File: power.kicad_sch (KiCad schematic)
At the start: 5 parts, among them J1 USB_C_Receptacle

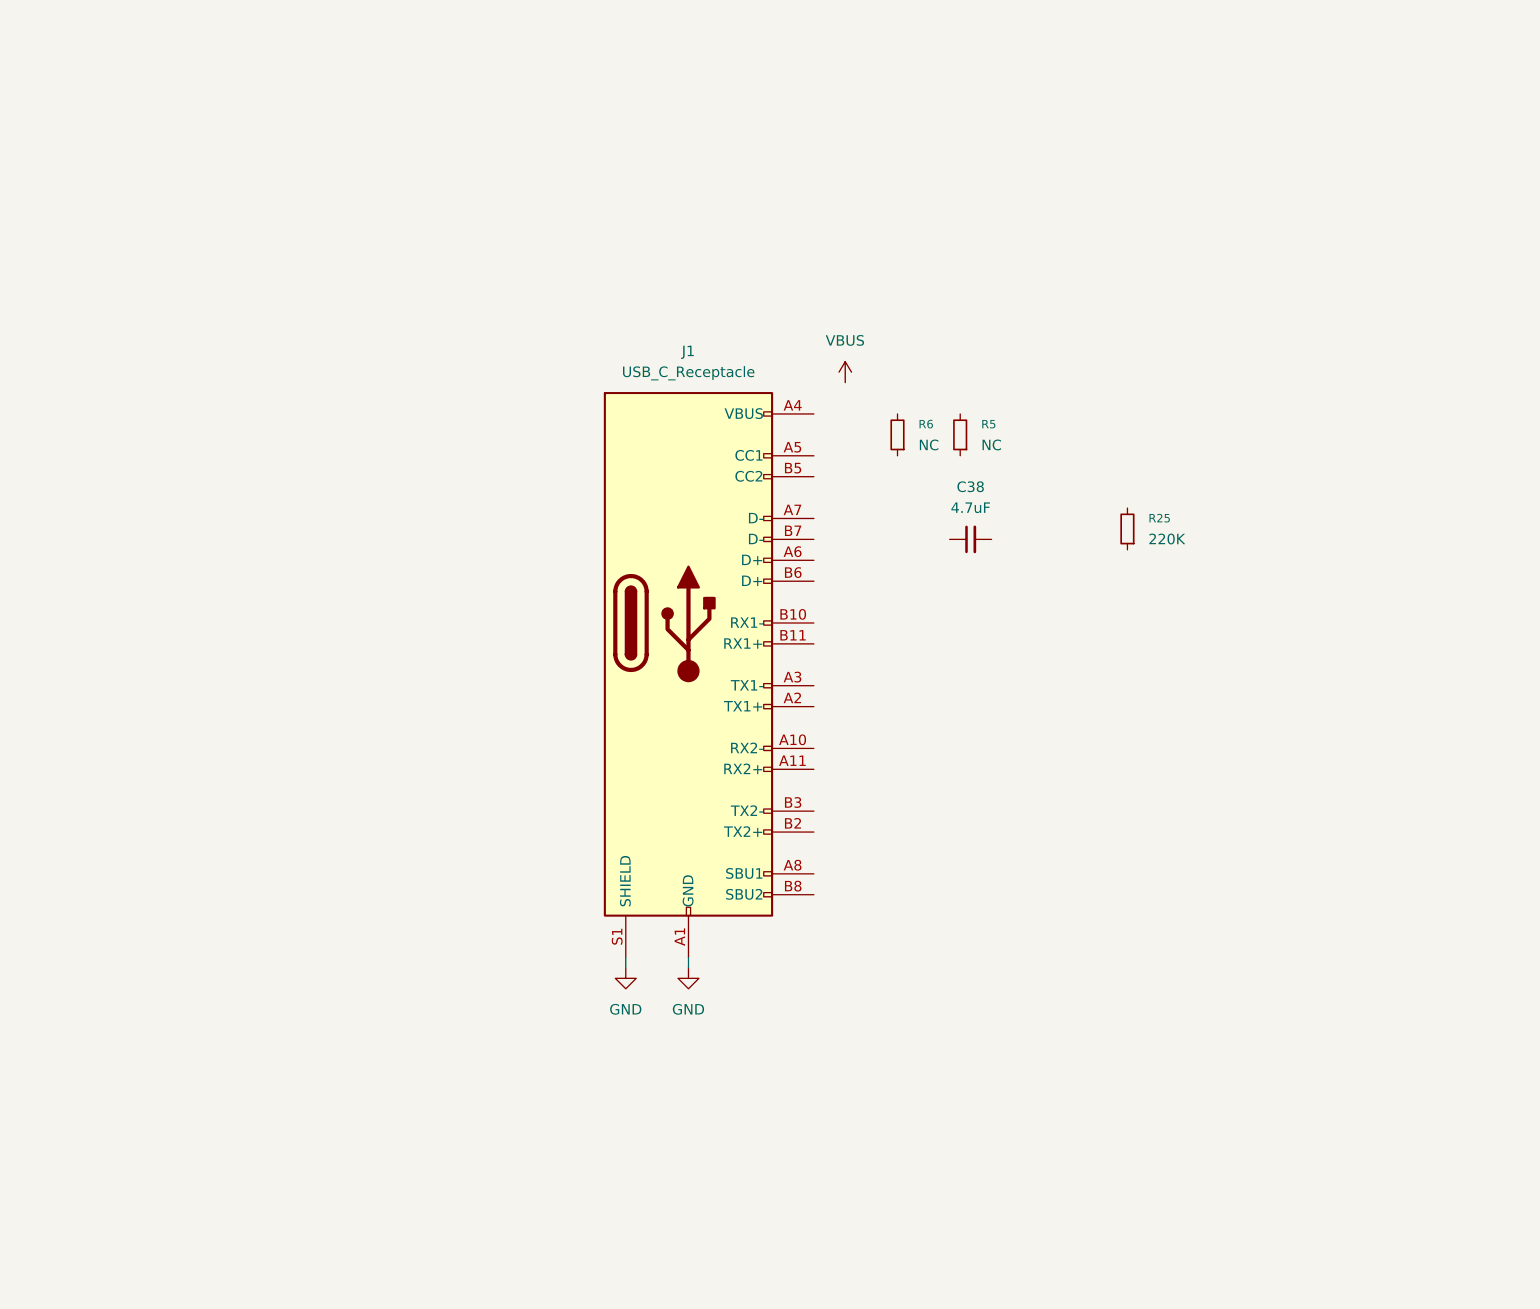
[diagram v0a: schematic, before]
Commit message: added power schematic, gitignore
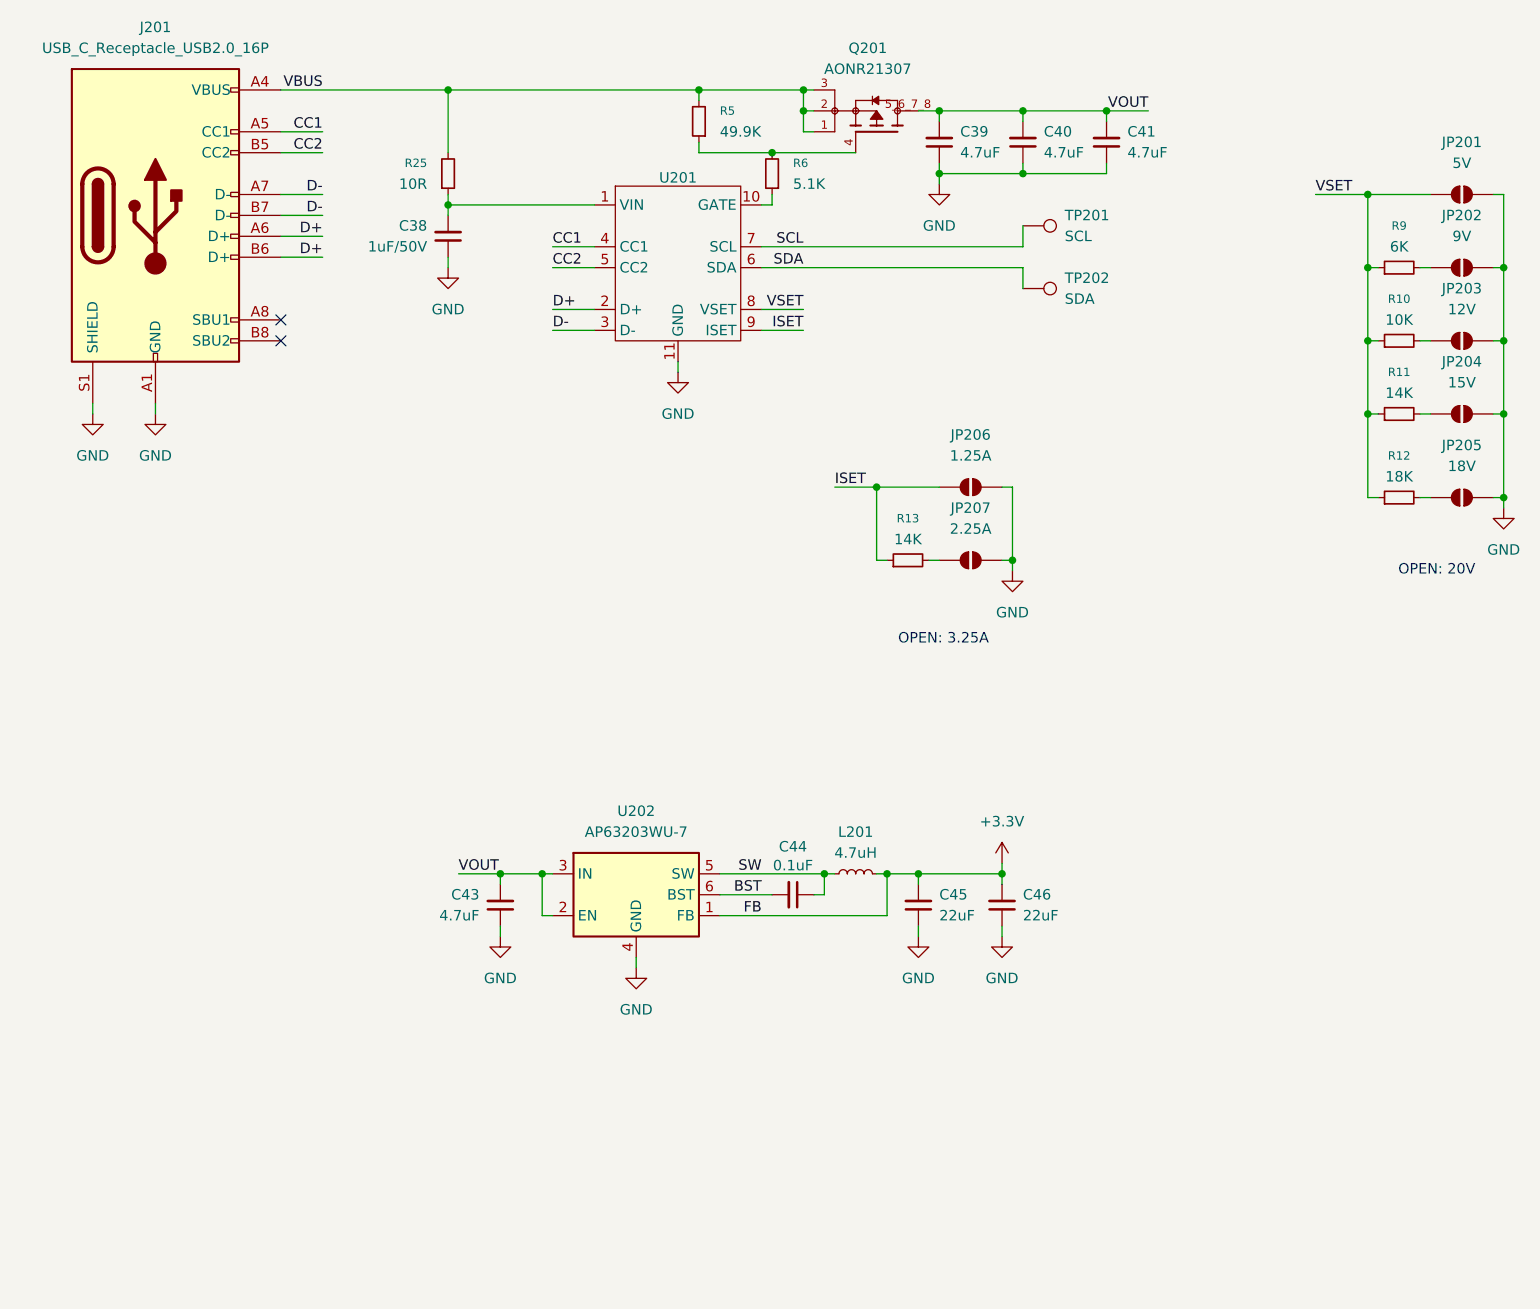
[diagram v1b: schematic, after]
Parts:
- removed J1: USB_C_Receptacle, symbol Connector:USB_C_Receptacle
- added C39, C40, C41, C43: 4.7uF, Capacitor_SMD:C_0603_1608Metric_Pad1.08x0.95mm_HandSolder, symbol Device:C_Small
- added C44: 0.1uF, Capacitor_SMD:C_0603_1608Metric_Pad1.08x0.95mm_HandSolder, symbol Device:C_Small
- added C45, C46: 22uF, Capacitor_SMD:C_0603_1608Metric_Pad1.08x0.95mm_HandSolder, symbol Device:C_Small
- added J201: USB_C_Receptacle_USB2.0_16P, SHOUHAN_TYPE-C_16PIN_2MD__073:SHOUHAN_TYPE-C_16PIN_2MD__073, symbol Connector:USB_C_Receptacle_USB2.0_16P
- added JP201: 5V, Jumper:SolderJumper-2_P1.3mm_Open_RoundedPad1.0x1.5mm, symbol Jumper:SolderJumper_2_Open
- added JP202: 9V, Jumper:SolderJumper-2_P1.3mm_Open_RoundedPad1.0x1.5mm, symbol Jumper:SolderJumper_2_Open
- added JP203: 12V, Jumper:SolderJumper-2_P1.3mm_Open_RoundedPad1.0x1.5mm, symbol Jumper:SolderJumper_2_Open
- added JP204: 15V, Jumper:SolderJumper-2_P1.3mm_Open_RoundedPad1.0x1.5mm, symbol Jumper:SolderJumper_2_Open
- added JP205: 18V, Jumper:SolderJumper-2_P1.3mm_Open_RoundedPad1.0x1.5mm, symbol Jumper:SolderJumper_2_Open
- added JP206: 1.25A, Jumper:SolderJumper-2_P1.3mm_Open_RoundedPad1.0x1.5mm, symbol Jumper:SolderJumper_2_Open
- added JP207: 2.25A, Jumper:SolderJumper-2_P1.3mm_Open_RoundedPad1.0x1.5mm, symbol Jumper:SolderJumper_2_Open
- added L201: 4.7uH, symbol Device:L_Small
- added Q201: AONR21307, AONR21307:AONR21307, symbol AONR21307:AONR21307
- added R10: 10K, Resistor_SMD:R_0603_1608Metric_Pad0.98x0.95mm_HandSolder, symbol Device:R_Small
- added R11, R13: 14K, Resistor_SMD:R_0603_1608Metric_Pad0.98x0.95mm_HandSolder, symbol Device:R_Small
- added R12: 18K, Resistor_SMD:R_0603_1608Metric_Pad0.98x0.95mm_HandSolder, symbol Device:R_Small
- added R9: 6K, Resistor_SMD:R_0603_1608Metric_Pad0.98x0.95mm_HandSolder, symbol Device:R_Small
- added TP201: SCL, TestPoint:TestPoint_Pad_D1.5mm, symbol Connector:TestPoint
- added TP202: SDA, TestPoint:TestPoint_Pad_D1.5mm, symbol Connector:TestPoint
- added U201: ~, Package_DFN_QFN:DFN-10-1EP_3x3mm_P0.5mm_EP1.55x2.48mm, symbol HUSB238_002DD:HUSB238_002DD
- added U202: AP63203WU-7, Package_TO_SOT_SMD:TSOT-23-6, symbol Regulator_Switching:AP63203WU
- C38: value 4.7uF -> 1uF/50V
- R25: value 220K -> 10R
- R5: value NC -> 49.9K
- R6: value NC -> 5.1K
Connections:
- net GND: now also C38.1, C39.1, C40.1, C41.1, C43.1, C45.1, C46.1, J201.A1 (GND), J201.A12 (GND), J201.B1 (GND), J201.B12 (GND), J201.S1 (SHIELD), JP201.2 (B), JP202.2 (B), JP203.2 (B), JP204.2 (B), JP205.2 (B), JP206.2 (B), JP207.2 (B), U201.11 (GND), U202.4 (GND)
- net VBUS: now also R25.2, R5.2, J201.A4 (VBUS), J201.A9 (VBUS), J201.B4 (VBUS), J201.B9 (VBUS), Q201.1, Q201.2, Q201.3
- net at R5.1: now also R6.2, Q201.4
- net at R25.1: now also C38.2, U201.1 (VIN)
- net at R6.1: now also U201.10 (GATE)
- new net: JP204.1 (A), R11.2
- new net: JP207.1 (A), R13.2
- new net: JP203.1 (A), R10.2
- new net: JP202.1 (A), R9.2
- new net: JP205.1 (A), R12.2
- new net +3.3V: C45.2, C46.2, L201.2, U202.1 (FB)
- new net BST: C44.2, U202.6 (BST)
- new net CC1: J201.A5 (CC1), U201.4 (CC1)
- new net CC2: J201.B5 (CC2), U201.5 (CC2)
- new net D+: J201.A6 (D+), J201.B6 (D+), U201.2 (D+)
- new net D-: J201.A7 (D-), J201.B7 (D-), U201.3 (D-)
- new net ISET: JP206.1 (A), R13.1, U201.9 (ISET)
- new net SCL: TP201.1, U201.7 (SCL)
- new net SDA: TP202.1, U201.6 (SDA)
- new net SW: C44.1, L201.1, U202.5 (SW)
- new net VOUT: C39.2, C40.2, C41.2, C43.2, Q201.5_6_7_8, U202.2 (EN), U202.3 (IN)
- new net VSET: JP201.1 (A), R10.1, R11.1, R12.1, R9.1, U201.8 (VSET)
- no-connect marks 0 -> 2
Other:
- note added: "OPEN: 20V"
- note added: "OPEN: 3.25A"
- moved on the sheet: C38, R25, R5, R6

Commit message: power section done
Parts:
- L201: value 4.7uH -> 10uH; footprint (none) -> VLS5045EX-100M:VLS5045EX330M
- U201: value ~ -> HUSB238_002DD; footprint Package_DFN_QFN:DFN-10-1EP_3x3mm_P0.5mm_EP1.55x2.48mm -> Package_DFN_QFN:DFN-10-1EP_3x3mm_P0.5mm_EP1.65x2.38mm_ThermalVias
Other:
- note added: "TDK, VLS5045EX-100M"
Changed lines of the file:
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@@
+		)
+	)
+	(text "TDK, VLS5045EX-100M"
+		(exclude_from_sim no)
+		(at 115.57 113.284 0)
+		(effects
+			(font
+				(size 1.27 1.27)
+			)
 		)
 	)
@@
 	)
 	(symbol
+		(lib_id "HUSB238_002DD:HUSB238_002DD")
+		(at 93.98 45.72 0)
+		(unit 1)
+		(exclude_from_sim no)
+		(in_bom yes)
+		(on_board yes)
+		(dnp no)
+		(property "Reference" "U201"
+			(at 93.98 33.782 0)
+			(effects
+				(font
+					(size 1.27 1.27)
+				)
+			)
+		)
+		(property "Value" "HUSB238_002DD"
+			(at 93.98 35.814 0)
+			(effects
+				(font
+					(size 1.27 1.27)
+				)
+			)
+		)
+		(property "Footprint" "Package_DFN_QFN:DFN-10-1EP_3x3mm_P0.5mm_EP1.65x2.38mm_ThermalVias"
+			(at 93.98 45.72 0)
+			(effects
+				(font
+					(size 1.27 1.27)
+				)
+				(hide yes)
+			)
+		)
+		(property "Datasheet" ""
+			(at 93.98 45.72 0)
+			(effects
+				(font
+					(size 1.27 1.27)
+				)
+				(hide yes)
+			)
+		)
+		(property "Description" ""
+			(at 93.98 45.72 0)
+			(effects
+				(font
+					(size 1.27 1.27)
+				)
+				(hide yes)
+			)
+		)
+		(pin "6"
+		)
+		(pin "3"
+		)
+		(pin "8"
+		)
+		(pin "2"
+		)
+		(pin "9"
+		)
+		(pin "7"
+		)
+		(pin "11"
+		)
+		(pin "1"
+		)
+		(pin "4"
+		)
+		(pin "5"
+		)
+		(pin "10"
+		)
+		(instances
+			(project ""
+				(path "/484c4955-80b8-457c-864e-1c65a3218727/bcad7757-d813-4960-9c64-164aa425f5cb"
+					(reference "U201")
+					(unit 1)
+				)
+			)
+		)
+	)
+	(symbol
 		(lib_id "power:GND")
 		(at 22.86 64.77 0)
@@
 			)
 		)
-		(property "Value" "4.7uH"
+		(property "Value" "10uH"
 			(at 115.57 118.11 90)
 			(effects
@@
 			)
 		)
-		(property "Footprint" ""
+		(property "Footprint" "VLS5045EX-100M:VLS5045EX330M"
 			(at 115.57 120.65 0)
 			(effects
@@
 					(unit 1)
 				)
-			)
-		)
-	)
-	(symbol
-		(lib_id "HUSB238_002DD:HUSB238_002DD")
-		(at 93.98 45.72 0)
-		(unit 1)
-		(exclude_from_sim no)
-		(in_bom yes)
-		(on_board yes)
-		(dnp no)
-		(property "Reference" "U201"
-			(at 93.98 36.068 0)
-			(effects
-				(font
-					(size 1.27 1.27)
-				)
-			)
-		)
-		(property "Value" "~"
-			(at 93.98 35.56 0)
-			(effects
-				(font
-					(size 1.27 1.27)
-				)
-			)
-		)
-		(property "Footprint" "Package_DFN_QFN:DFN-10-1EP_3x3mm_P0.5mm_EP1.55x2.48mm"
-			(at 93.98 45.72 0)
-			(effects
-				(font
-					(size 1.27 1.27)
-				)
-				(hide yes)
-			)
-		)
-		(property "Datasheet" ""
-			(at 93.98 45.72 0)
-			(effects
-				(font
-					(size 1.27 1.27)
-				)
-				(hide yes)
-			)
-		)
-		(property "Description" ""
-			(at 93.98 45.72 0)
-			(effects
-				(font
-					(size 1.27 1.27)
-				)
-				(hide yes)
-			)
-		)
-		(pin "4"
-		)
-		(pin "11"
-		)
-		(pin "8"
-		)
-		(pin "5"
-		)
-		(pin "2"
-		)
-		(pin "1"
-		)
-		(pin "3"
-		)
-		(pin "10"
-		)
-		(pin "6"
-		)
-		(pin "7"
-		)
-		(pin "9"
-		)
-		(instances
-			(project ""
-				(path "/484c4955-80b8-457c-864e-1c65a3218727/bcad7757-d813-4960-9c64-164aa425f5cb"
-					(reference "U201")
-					(unit 1)
-				)

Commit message: schematic completed
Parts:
- added D403: 3.3V, LED_SMD:LED_0603_1608Metric_Pad1.05x0.95mm_HandSolder, symbol Device:LED_Small
- added D404: VDD, LED_SMD:LED_0603_1608Metric_Pad1.05x0.95mm_HandSolder, symbol Device:LED_Small
- added J202: J, Connector_PinSocket_2.54mm:PinSocket_1x02_P2.54mm_Vertical, symbol Connector_Generic:Conn_01x02
- added R37, R38: 1K, Resistor_SMD:R_0603_1608Metric_Pad0.98x0.95mm_HandSolder, symbol Device:R_Small
- added TP307: VBUS, TestPoint:TestPoint_THTPad_1.0x1.0mm_Drill0.5mm, symbol Connector:TestPoint
- added TP308: VOUT, TestPoint:TestPoint_THTPad_1.0x1.0mm_Drill0.5mm, symbol Connector:TestPoint
- added TP309: 3.3V, TestPoint:TestPoint_THTPad_1.0x1.0mm_Drill0.5mm, symbol Connector:TestPoint
- added TP310: VDD, TestPoint:TestPoint_THTPad_1.0x1.0mm_Drill0.5mm, symbol Connector:TestPoint
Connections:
- net +3.3V: now also J202.1 (Pin_1), R37.2, TP309.1
- net GND: now also D403.1 (K), D404.1 (K)
- net VBUS: now also TP307.1
- net VOUT: now also TP308.1
- new net: D404.2 (A), R38.1
- new net: D403.2 (A), R37.1
- new net VDD: J202.2 (Pin_2), R38.2, TP310.1

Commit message: FINALISED LAYOUT
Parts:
- renumbered C39 to C201, C40 to C202, C41 to C203, C38 to C204, C44 to C205, C43 to C206, C45 to C207, C46 to C208, D403 to D201, D404 to D202, JP206 to JP205, JP205 to JP206, R5 to R201, R25 to R202, R6 to R203, R9 to R204, R10 to R205, R11 to R206, R12 to R207, R13 to R208, R37 to R209, R38 to R210, TP307 to TP201, TP201 to TP202, TP202 to TP203, TP308 to TP204, TP309 to TP205, TP310 to TP206

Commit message: finalised layout
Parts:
- renumbered C201 to C1, C202 to C2, C203 to C3, C204 to C4, C205 to C5, C206 to C6, C207 to C7, C208 to C8, D201 to D1, D202 to D2, J201 to J1, J202 to J2, JP201 to JP1, JP202 to JP2, JP203 to JP3, JP204 to JP4, JP205 to JP5, JP206 to JP6, JP207 to JP7, L201 to L1, Q201 to Q1, R201 to R1, R210 to R10, R202 to R2, R203 to R3, R204 to R4, R205 to R5, R206 to R6, R207 to R7, R208 to R8, R209 to R9, TP201 to TP1, TP202 to TP2, TP203 to TP3, TP204 to TP4, TP205 to TP5, TP206 to TP6, U201 to U1, U202 to U2

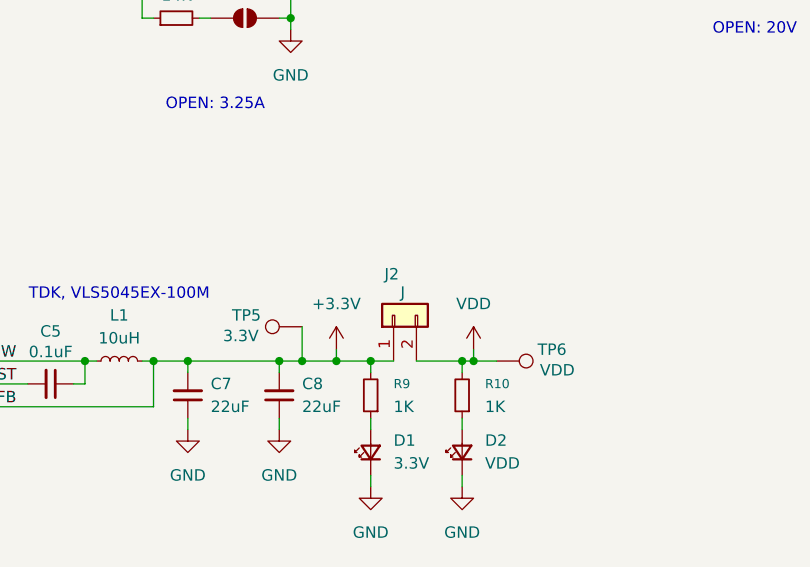
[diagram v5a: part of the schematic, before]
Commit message: fixed ground pour
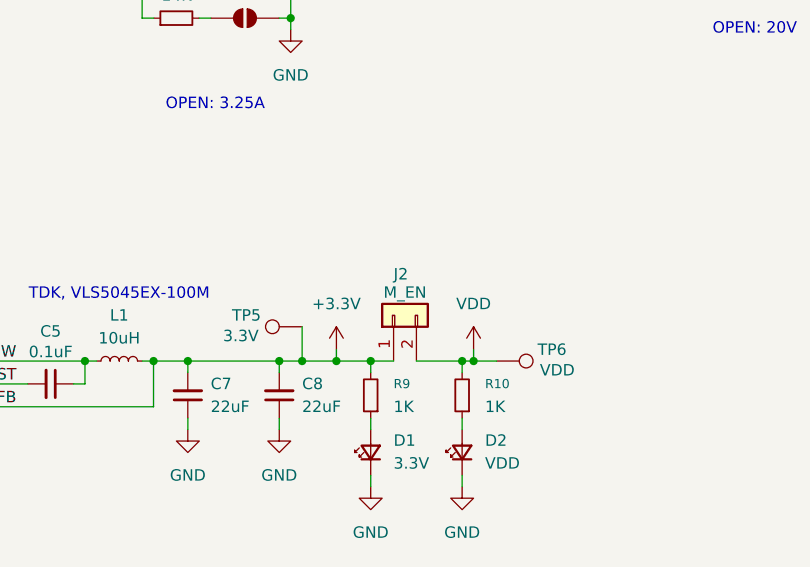
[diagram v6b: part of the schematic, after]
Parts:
- J2: value J -> M_EN
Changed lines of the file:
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@@
 		(dnp no)
 		(property "Reference" "J2"
-			(at 145.034 110.998 90)
+			(at 146.05 110.998 90)
 			(effects
 				(font
@@
 			)
 		)
-		(property "Value" "J"
-			(at 146.812 113.03 90)
+		(property "Value" "M_EN"
+			(at 147.32 113.03 90)
 			(effects
 				(font
 					(size 1.27 1.27)
 				)
-				(justify right)
 			)
 		)
